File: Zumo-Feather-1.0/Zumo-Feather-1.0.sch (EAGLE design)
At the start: 2 parts, among them U1 ARDUINOR3-DIMENSION

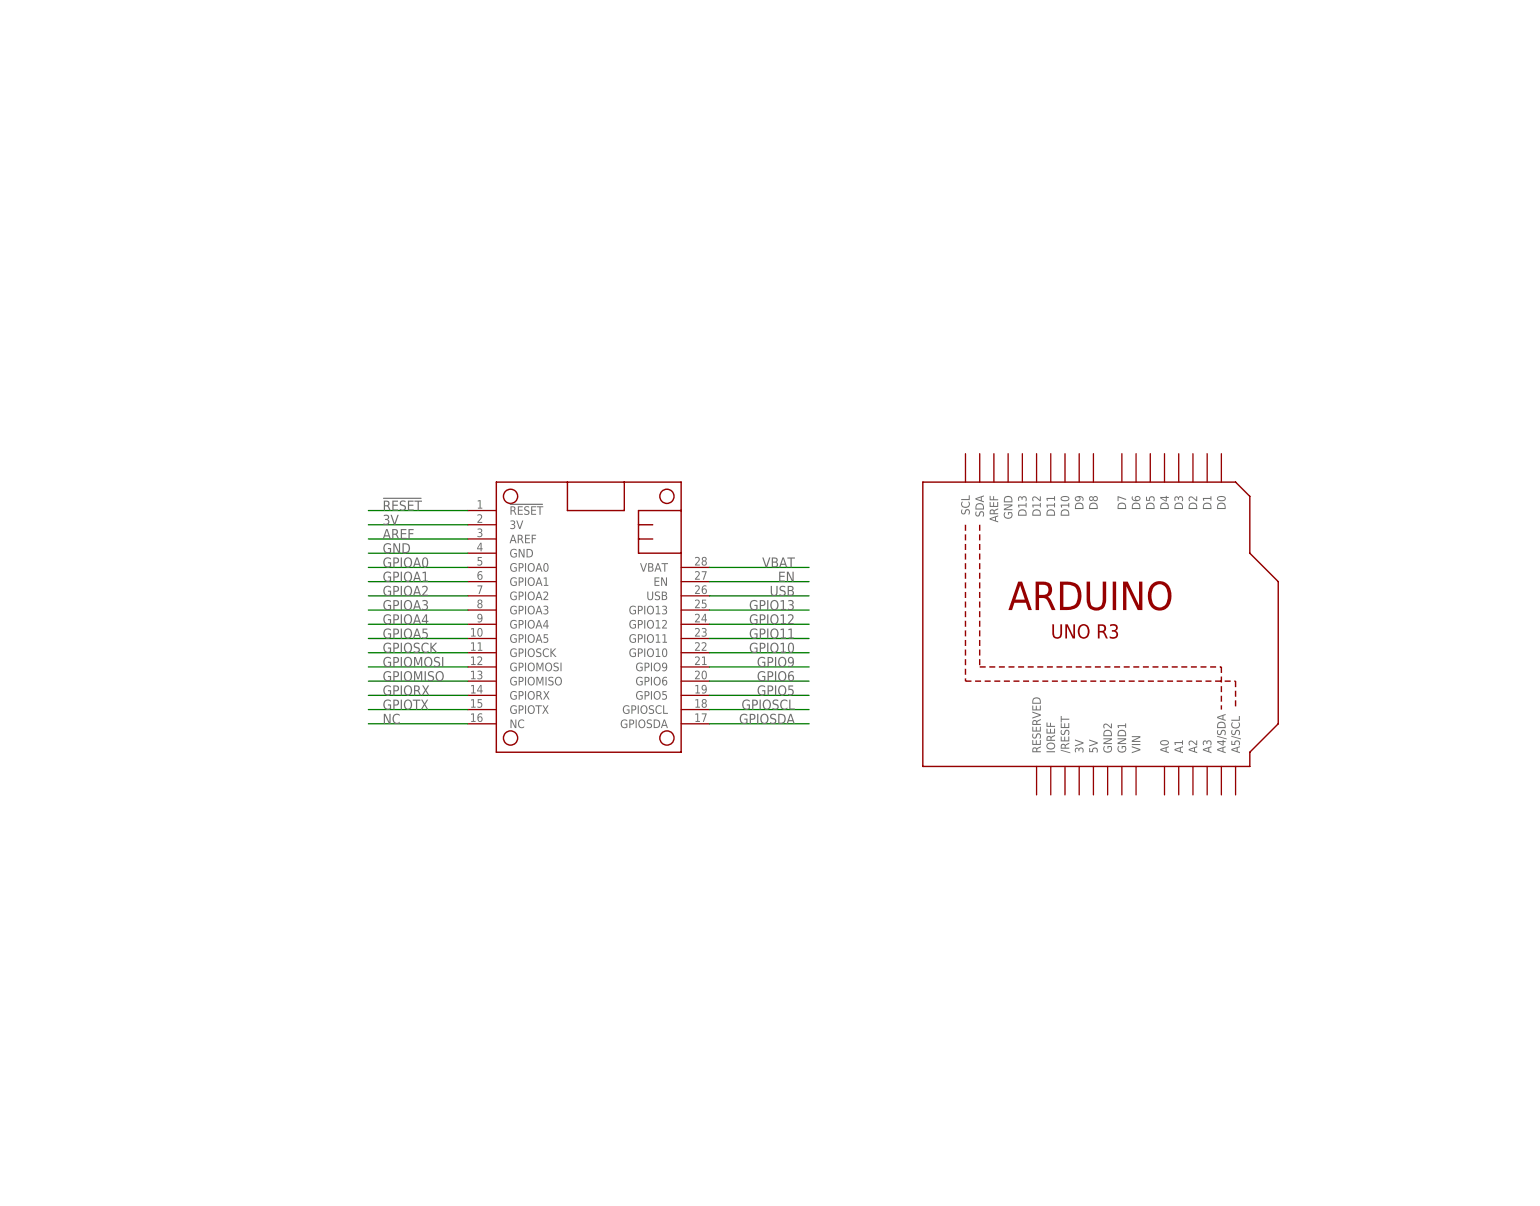
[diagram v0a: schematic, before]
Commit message: Added CAD and worked on Feather-Zumo Interface board
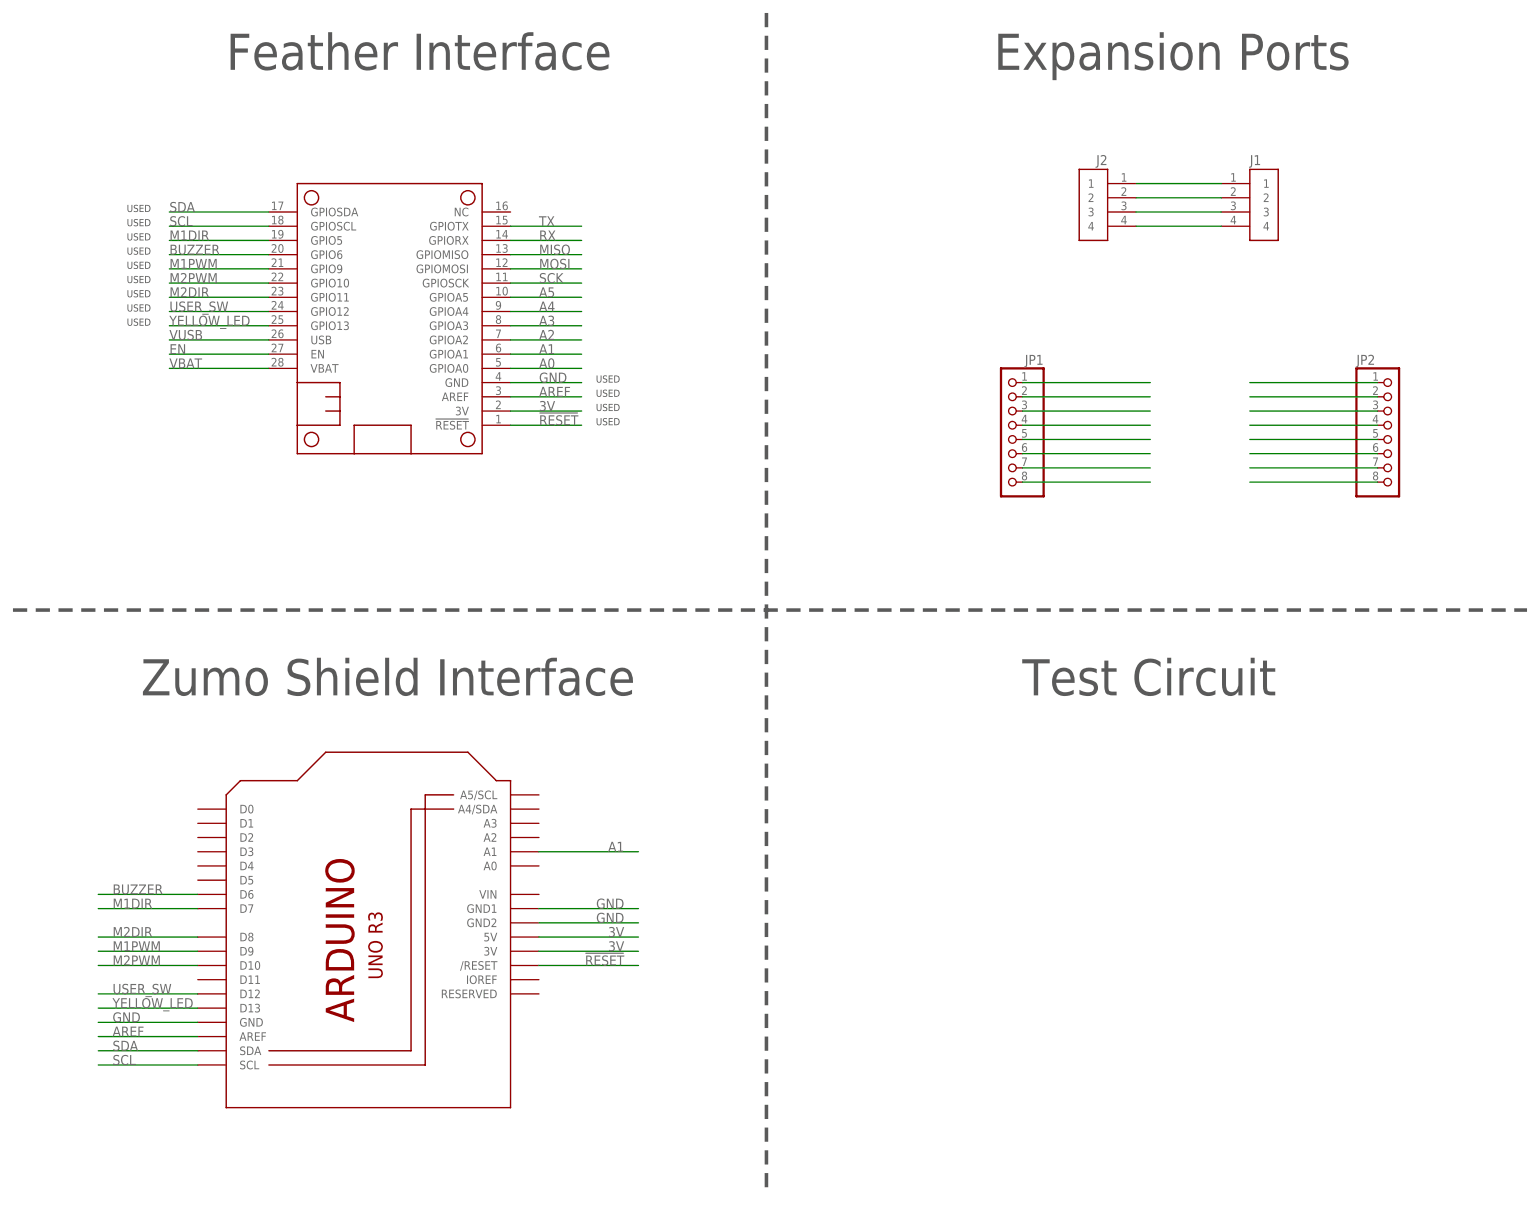
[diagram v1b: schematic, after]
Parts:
- added J1, J2: (no value), AIMRL:CON-SM04B-SRSS-TB
- added JP1, JP2: (no value), pinhead:PINHD-1X8
- MS1: value FEATHERWING_NODIM -> BRD-FEATHERWING_NODIM; device adafruit:FEATHERWING_NODIM -> AIMRL:BRD-FEATHERWING_NODIM
- U1: value ARDUINOR3-DIMENSION -> BRD-ARDUINOR3-DIMENSION; device adafruit:ARDUINOR3-DIMENSION -> AIMRL:BRD-ARDUINOR3-DIMENSION
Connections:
- net GPIOA0 renamed A0
- net GPIOA2 renamed A2
- net GPIOA3 renamed A3
- net GPIOA4 renamed A4
- net GPIOA5 renamed A5
- net GPIOMISO renamed MISO
- net GPIOMOSI renamed MOSI
- net GPIORX renamed RX
- net GPIOSCK renamed SCK
- net GPIOTX renamed TX
- net USB renamed VUSB
- removed net GPIO10: MS1.GPIO10
- removed net GPIO11: MS1.GPIO11
- removed net GPIO12: MS1.GPIO12
- removed net GPIO13: MS1.GPIO13
- removed net GPIO5: MS1.GPIO5
- removed net GPIO6: MS1.GPIO6
- removed net GPIO9: MS1.GPIO9
- removed net GPIOA1: MS1.GPIOA1
- removed net GPIOSCL: MS1.GPIOSCL
- removed net GPIOSDA: MS1.GPIOSDA
- removed net NC: MS1.NC
- new net A1: MS1.GPIOA1, U1.A1
- new net BUZZER: MS1.GPIO6, U1.D6
- new net M1DIR: MS1.GPIO5, U1.D7
- new net M1PWM: MS1.GPIO9, U1.D9
- new net M2DIR: MS1.GPIO11, U1.D8
- new net M2PWM: MS1.GPIO10, U1.D10
- new net N$1: J1.1, J2.1
- new net N$10: JP2.6
- new net N$11: JP2.7
- new net N$12: JP2.8
- new net N$13: JP1.1
- new net N$14: JP1.2
- new net N$15: JP1.3
- new net N$16: JP1.4
- new net N$17: JP1.5
- new net N$18: JP1.6
- new net N$19: JP1.7
- new net N$2: J1.2, J2.2
- new net N$20: JP1.8
- new net N$3: J1.3, J2.3
- new net N$4: J1.4, J2.4
- new net N$5: JP2.1
- new net N$6: JP2.2
- new net N$7: JP2.3
- new net N$8: JP2.4
- new net N$9: JP2.5
- new net SCL: MS1.GPIOSCL, U1.SCL
- new net SDA: MS1.GPIOSDA, U1.SDA
- new net USER_SW: MS1.GPIO12, U1.D12
- new net YELLOW_LED: MS1.GPIO13, U1.D13
- net !RESET: now also U1./RESET
- net 3V: now also U1.3V, U1.5V
- net AREF: now also U1.AREF
- net GND: now also U1.GND, U1.GND1, U1.GND2
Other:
- note added: "Expansion Ports"
- note added: "Feather Interface"
- note added: "Test Circuit"
- note added: "USED"
- note added: "Zumo Shield Interface"

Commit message: Worked on Zumo board
Swapped pinout around a bunch to make layout easier. Realized power is provided by a 7.5V boost converter, which is not ideal. I will need to jumper VBATT directly from the Zumo Shield or bypass the boost converter.
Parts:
- added JP3: (no value), pinhead:PINHD-1X2
- added R1: (no value), RLC:R-US_R0805
- MS1: value BRD-FEATHERWING_NODIM -> BRD-FEATHERWING_NODIM_NOMNT; device AIMRL:BRD-FEATHERWING_NODIM -> AIMRL:BRD-FEATHERWING_NODIM_NOMNT
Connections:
- removed net A0: MS1.GPIOA0
- removed net A2: MS1.GPIOA2
- removed net A3: MS1.GPIOA3
- removed net A4: MS1.GPIOA4
- removed net A5: MS1.GPIOA5
- removed net N$1: J1.1, J2.1
- removed net N$2: J1.2, J2.2
- removed net N$3: J1.3, J2.3
- removed net N$4: J1.4, J2.4
- new net GPIO10: MS1.GPIO10
- new net GPIO11: MS1.GPIO11
- new net GPIO12: MS1.GPIO12
- new net GPIO13: MS1.GPIO13
- new net GPIO6: MS1.GPIO6
- new net GPIO9: MS1.GPIO9
- new net VIN: R1.2, U1.VIN
- net 3V: now also J1.2, J2.2
- net A1: no longer MS1.GPIOA1
- net BUZZER: now also MS1.GPIO5; no longer MS1.GPIO6
- net GND: now also J1.1, J2.1, JP3.2
- net M1DIR: now also MS1.GPIOA5; no longer MS1.GPIO5
- net M1PWM: now also MS1.GPIOA3; no longer MS1.GPIO9
- net M2DIR: now also MS1.GPIOA4; no longer MS1.GPIO11
- net M2PWM: now also MS1.GPIOA2; no longer MS1.GPIO10
- net SCL: now also J1.4, J2.4
- net SDA: now also J1.3, J2.3
- net USER_SW: now also MS1.GPIOA1; no longer MS1.GPIO12
- net VBAT: now also JP3.1, R1.1
- net YELLOW_LED: now also MS1.GPIOA0; no longer MS1.GPIO13
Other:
- note added: "Power Options: 1) Batteries in Zumo a) boost bypassed:"
- note added: "VBAT to VIN jumper"
- note added: "VBAT/GND connector for powering Zumo motors directly from Feather Li-Ion or VUSB"
- note added: "only populate if boost regulator on Zumo Shield has been bypassed."

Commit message: Updated schematic
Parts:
- removed R1: (no value), RLC:R-US_R0805
- added JP4: (no value), pinhead:PINHD-1X2
- JP1: device pinhead:PINHD-1X8 -> pinhead:PINHD-2X3
- JP2: device pinhead:PINHD-1X8 -> pinhead:PINHD-2X2
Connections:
- removed net N$10: JP2.6
- removed net N$11: JP2.7
- removed net N$12: JP2.8
- removed net N$13: JP1.1
- removed net N$14: JP1.2
- removed net N$15: JP1.3
- removed net N$16: JP1.4
- removed net N$17: JP1.5
- removed net N$18: JP1.6
- removed net N$19: JP1.7
- removed net N$20: JP1.8
- removed net N$5: JP2.1
- removed net N$6: JP2.2
- removed net N$7: JP2.3
- removed net N$8: JP2.4
- removed net N$9: JP2.5
- net 3V: now also JP1.2, JP2.4
- net GND: now also JP1.6, JP2.2
- net GPIO13: now also JP1.4
- net MISO: now also JP1.1
- net MOSI: now also JP1.3
- net RX: now also JP2.3
- net SCK: now also JP1.5
- net TX: now also JP2.1
- net VBAT: now also JP4.1; no longer R1.1
- net VIN: now also JP4.2; no longer R1.2
